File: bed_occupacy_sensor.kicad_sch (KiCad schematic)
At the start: 4 parts, among them U1 mini_esp32

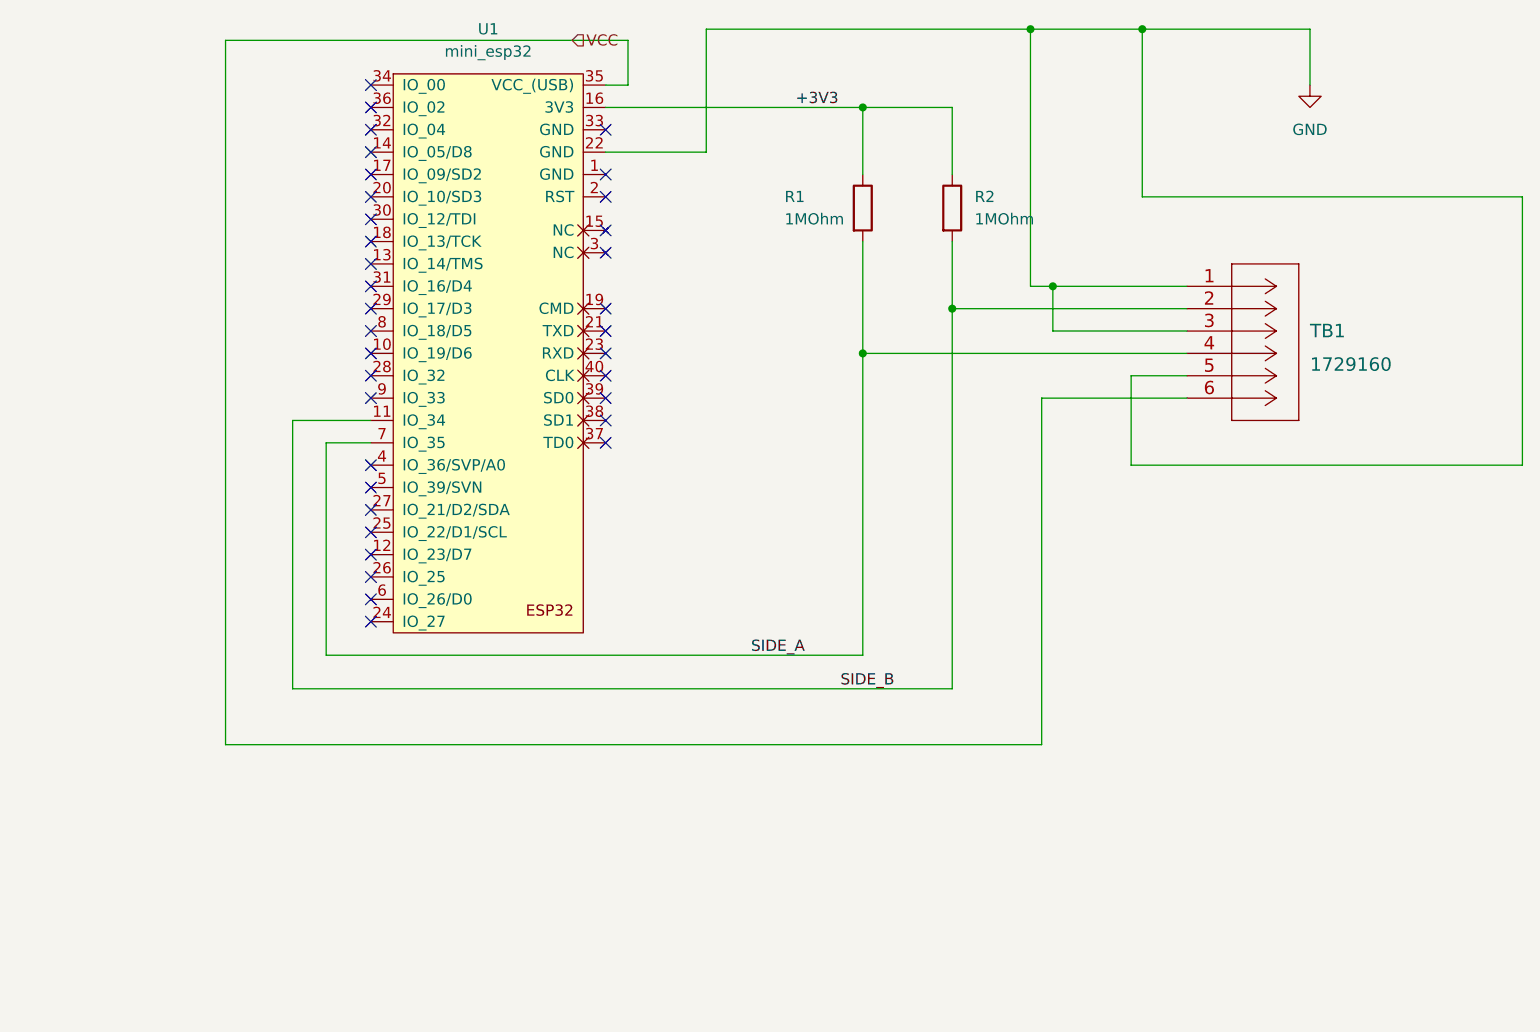
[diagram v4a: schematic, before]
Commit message: Reverse the footprint of ESP, as it was the wrong way around
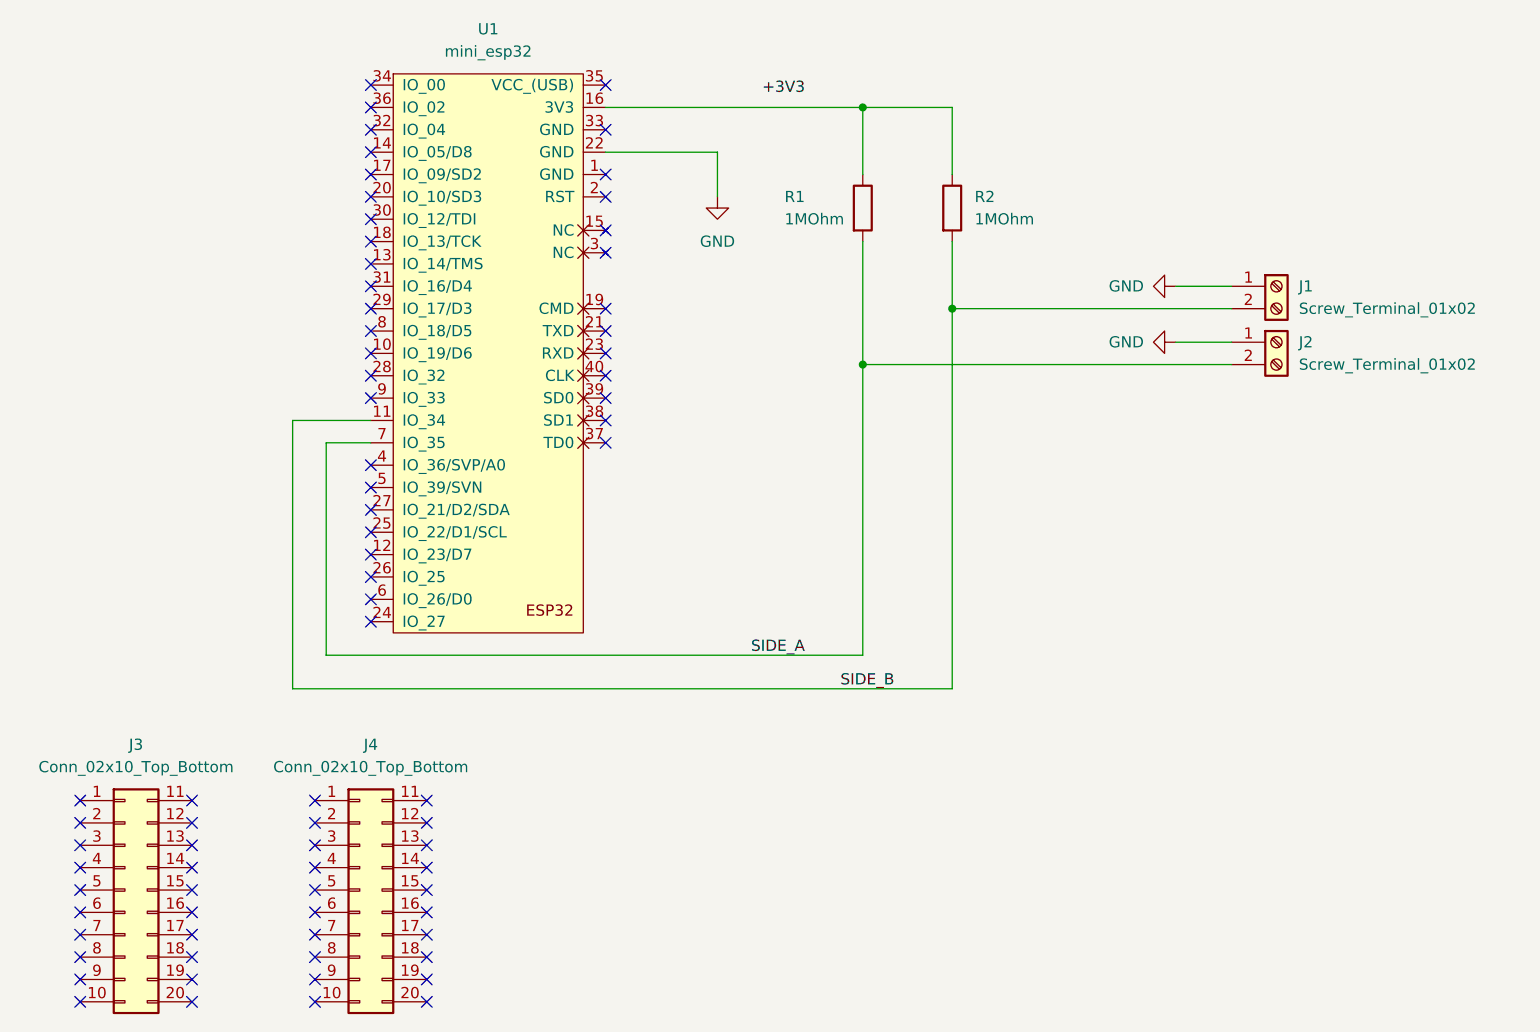
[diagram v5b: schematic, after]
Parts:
- removed TB1: 1729160, TerminalBlock_Phoenix:TerminalBlock_Phoenix_MKDS-1,5-6-5.08_1x06_P5.08mm_Horizontal, symbol phoenixcontact_1729160:1729160
- added J1, J2: Screw_Terminal_01x02, TerminalBlock_Phoenix:TerminalBlock_Phoenix_MKDS-1,5-2-5.08_1x02_P5.08mm_Horizontal, symbol Connector:Screw_Terminal_01x02
- added J3, J4: Conn_02x10_Top_Bottom, Connector_PinSocket_2.54mm:PinSocket_2x10_P2.54mm_Vertical, symbol Connector_Generic:Conn_02x10_Top_Bottom
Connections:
- net +3V3: no longer R1.1, R2.1, U1.16 (3V3)
- net GND: now also J1.1 (Pin_1), J2.1 (Pin_1)
- net SIDE_A: now also J2.2 (Pin_2)
- net SIDE_B: now also J1.2 (Pin_2)
- net VCC: no longer names the net of U1.35 (VCC_(USB))
- new net: R1.1, R2.1, U1.16 (3V3)
- no-connect marks 35 -> 76

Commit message: fixed design flaw of ESP-Pin orientation (it was the wrong way around). Now the antenna is free (on it's downside) removed QR Code because it's too small to read by a QR-Code-Reader. Updated the resistor footprint to a smaller one (10,4mm) because it fits better to standard metal-film resistors
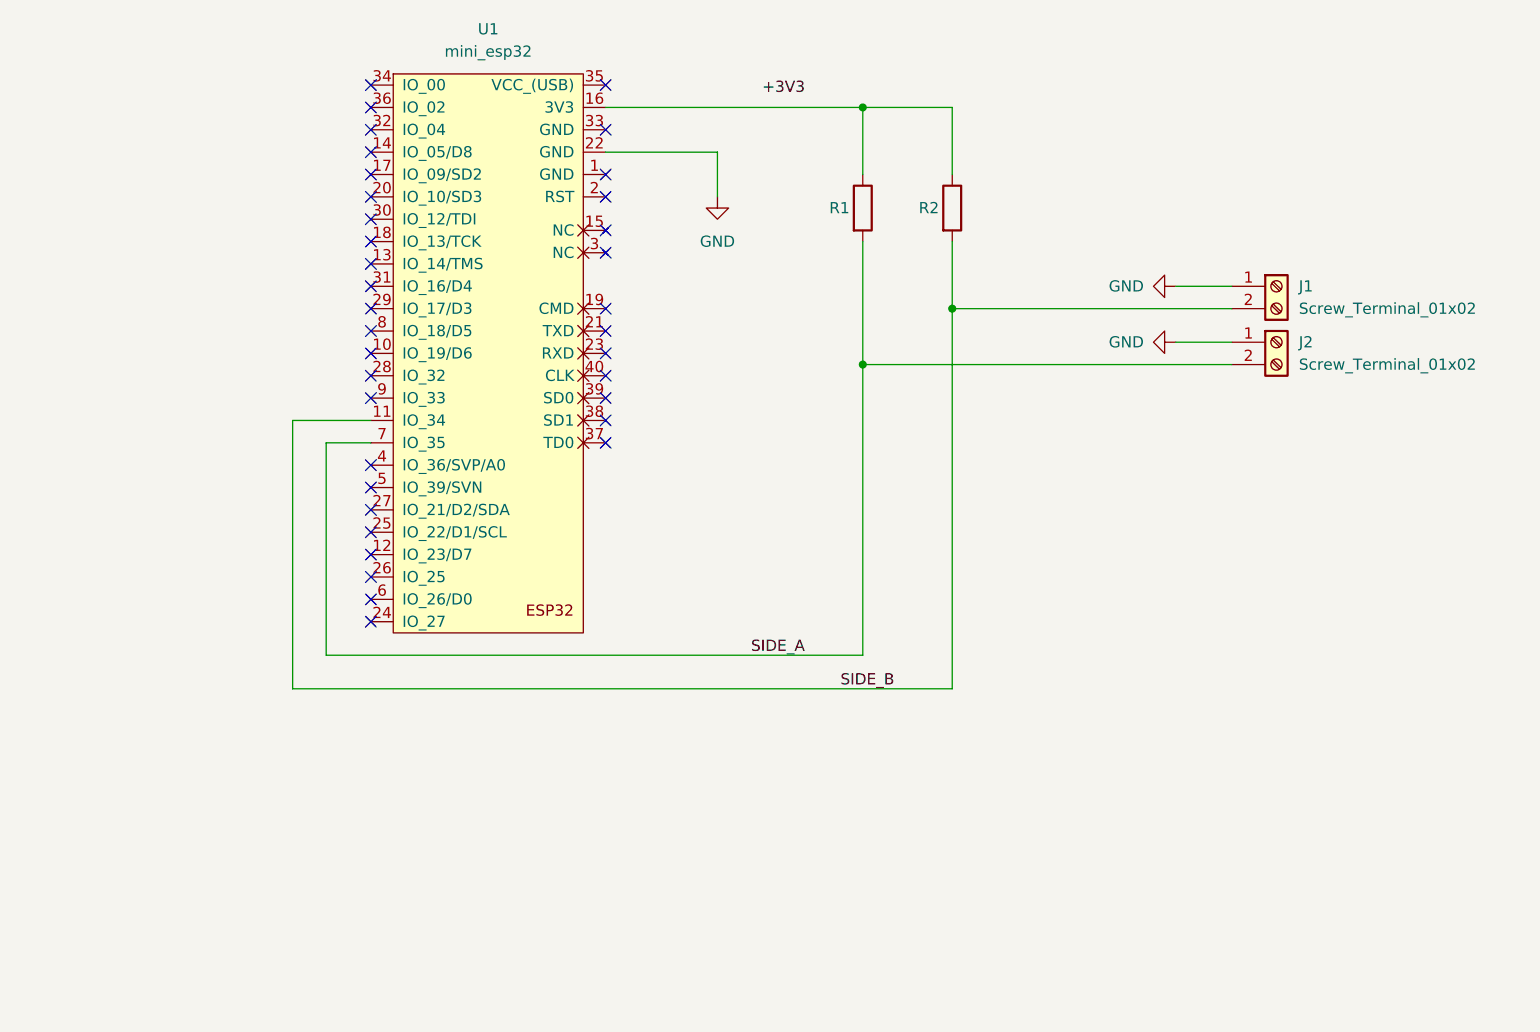
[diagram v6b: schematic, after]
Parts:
- removed J3, J4: Conn_02x10_Top_Bottom, Connector_PinSocket_2.54mm:PinSocket_2x10_P2.54mm_Vertical, symbol Connector_Generic:Conn_02x10_Top_Bottom
- R1, R2: value 1MOhm -> to be calculated; footprint Resistor_THT:R_Axial_DIN0207_L6.3mm_D2.5mm_P15.24mm_Horizontal -> Resistor_THT:R_Axial_DIN0207_L6.3mm_D2.5mm_P10.16mm_Horizontal
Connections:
- no-connect marks 76 -> 36
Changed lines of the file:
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@@
   )
   (no_connect (at 57.15 69.85))
+  (no_connect (at 83.82 24.13))
   (no_connect (at 57.15 26.67))
-  (no_connect (at 24.13 110.49))
-  (no_connect (at 83.82 24.13))
-  (no_connect (at 63.5 125.73))
-  (no_connect (at 24.13 113.03))
-  (no_connect (at 36.83 105.41))
-  (no_connect (at 63.5 113.03))
-  (no_connect (at 63.5 123.19))
-  (no_connect (at 36.83 115.57))
-  (no_connect (at 50.8 120.65))
   (no_connect (at 57.15 59.69))
-  (no_connect (at 50.8 118.11))
   (no_connect (at 57.15 57.15))
   (no_connect (at 83.82 64.77))
@@
   (no_connect (at 57.15 77.47))
   (no_connect (at 83.82 59.69))
-  (no_connect (at 63.5 107.95))
   (no_connect (at 57.15 36.83))
   (no_connect (at 57.15 29.21))
   (no_connect (at 83.82 29.21))
-  (no_connect (at 24.13 123.19))
-  (no_connect (at 36.83 107.95))
-  (no_connect (at 63.5 110.49))
   (no_connect (at 83.82 54.61))
   (no_connect (at 57.15 74.93))
-  (no_connect (at 24.13 128.27))
   (no_connect (at 83.82 52.07))
-  (no_connect (at 63.5 128.27))
-  (no_connect (at 36.83 120.65))
   (no_connect (at 83.82 62.23))
-  (no_connect (at 50.8 105.41))
   (no_connect (at 57.15 52.07))
-  (no_connect (at 36.83 118.11))
-  (no_connect (at 50.8 125.73))
-  (no_connect (at 63.5 120.65))
-  (no_connect (at 36.83 128.27))
-  (no_connect (at 24.13 107.95))
-  (no_connect (at 63.5 118.11))
-  (no_connect (at 36.83 125.73))
   (no_connect (at 83.82 40.64))
   (no_connect (at 57.15 80.01))
   (no_connect (at 57.15 54.61))
-  (no_connect (at 24.13 105.41))
   (no_connect (at 57.15 41.91))
-  (no_connect (at 24.13 125.73))
-  (no_connect (at 24.13 118.11))
-  (no_connect (at 50.8 123.19))
-  (no_connect (at 50.8 113.03))
-  (no_connect (at 36.83 123.19))
-  (no_connect (at 63.5 105.41))
   (no_connect (at 57.15 31.75))
   (no_connect (at 57.15 72.39))
   (no_connect (at 57.15 44.45))
-  (no_connect (at 24.13 120.65))
-  (no_connect (at 24.13 115.57))
-  (no_connect (at 50.8 107.95))
   (no_connect (at 57.15 34.29))
   (no_connect (at 83.82 57.15))
@@
   (no_connect (at 57.15 39.37))
   (no_connect (at 83.82 34.29))
-  (no_connect (at 36.83 110.49))
-  (no_connect (at 63.5 115.57))
-  (no_connect (at 50.8 128.27))
-  (no_connect (at 50.8 110.49))
   (no_connect (at 83.82 49.53))
   (no_connect (at 57.15 49.53))
-  (no_connect (at 50.8 115.57))
   (no_connect (at 57.15 85.09))
   (no_connect (at 83.82 43.18))
   (no_connect (at 83.82 36.83))
-  (no_connect (at 36.83 113.03))
   (no_connect (at 57.15 24.13))
   (no_connect (at 57.15 67.31))
@@
     (pin "9")
   )
-  (symbol (lib_id "Connector_Generic:Conn_02x10_Top_Bottom") (at 55.88 115.57 0) (unit 1)
-    (in_bom yes) (on_board yes) (fields_autoplaced)
-    (property "Reference" "J4" (id 0) (at 57.15 99.06 0))
-    (property "Value" "Conn_02x10_Top_Bottom" (id 1) (at 57.15 101.6 0))
-    (property "Footprint" "Connector_PinSocket_2.54mm:PinSocket_2x10_P2.54mm_Vertical" (id 2) (at 55.88 115.57 0)
-      (effects (font (size 1.27 1.27)) hide)
-    )
-    (property "Datasheet" "~" (id 3) (at 55.88 115.57 0)
-      (effects (font (size 1.27 1.27)) hide)
-    )
-    (pin "1")
-    (pin "10")
-    (pin "11")
-    (pin "12")
-    (pin "13")
-    (pin "14")
-    (pin "15")
-    (pin "16")
-    (pin "17")
-    (pin "18")
-    (pin "19")
-    (pin "2")
-    (pin "20")
-    (pin "3")
-    (pin "4")
-    (pin "5")
-    (pin "6")
-    (pin "7")
-    (pin "8")
-    (pin "9")
-  )
   (symbol (lib_id "Connector:Screw_Terminal_01x02") (at 160.02 53.34 0) (unit 1)
     (in_bom yes) (on_board yes) (fields_autoplaced)
@@
   (symbol (lib_id "Device:R") (at 113.03 38.1 0) (unit 1)
     (in_bom yes) (on_board yes)
-    (property "Reference" "R1" (id 0) (at 104.14 36.83 0)
-      (effects (font (size 1.27 1.27)) (justify left))
-    )
-    (property "Value" "1MOhm" (id 1) (at 104.14 39.37 0)
-      (effects (font (size 1.27 1.27)) (justify left))
-    )
-    (property "Footprint" "Resistor_THT:R_Axial_DIN0207_L6.3mm_D2.5mm_P15.24mm_Horizontal" (id 2) (at 111.252 38.1 90)
+    (property "Reference" "R1" (id 0) (at 109.22 38.1 0)
+      (effects (font (size 1.27 1.27)) (justify left))
+    )
+    (property "Value" "to be calculated" (id 1) (at 109.22 45.72 90)
+      (effects (font (size 1.27 1.27)) (justify left) hide)
+    )
+    (property "Footprint" "Resistor_THT:R_Axial_DIN0207_L6.3mm_D2.5mm_P10.16mm_Horizontal" (id 2) (at 111.252 38.1 90)
       (effects (font (size 1.27 1.27)) hide)
     )
@@
   )
   (symbol (lib_id "Device:R") (at 123.19 38.1 0) (unit 1)
-    (in_bom yes) (on_board yes) (fields_autoplaced)
-    (property "Reference" "R2" (id 0) (at 125.73 36.8299 0)
-      (effects (font (size 1.27 1.27)) (justify left))
-    )
-    (property "Value" "1MOhm" (id 1) (at 125.73 39.3699 0)
-      (effects (font (size 1.27 1.27)) (justify left))
-    )
-    (property "Footprint" "Resistor_THT:R_Axial_DIN0207_L6.3mm_D2.5mm_P15.24mm_Horizontal" (id 2) (at 121.412 38.1 90)
+    (in_bom yes) (on_board yes)
+    (property "Reference" "R2" (id 0) (at 119.38 38.1 0)
+      (effects (font (size 1.27 1.27)) (justify left))
+    )
+    (property "Value" "to be calculated" (id 1) (at 125.73 39.3699 0)
+      (effects (font (size 1.27 1.27)) (justify left) hide)
+    )
+    (property "Footprint" "Resistor_THT:R_Axial_DIN0207_L6.3mm_D2.5mm_P10.16mm_Horizontal" (id 2) (at 121.412 38.1 90)
       (effects (font (size 1.27 1.27)) hide)
     )
@@
     )
     (pin "1")
-  )
-  (symbol (lib_id "Connector_Generic:Conn_02x10_Top_Bottom") (at 29.21 115.57 0) (unit 1)
-    (in_bom yes) (on_board yes) (fields_autoplaced)
-    (property "Reference" "J3" (id 0) (at 30.48 99.06 0))
-    (property "Value" "Conn_02x10_Top_Bottom" (id 1) (at 30.48 101.6 0))
-    (property "Footprint" "Connector_PinSocket_2.54mm:PinSocket_2x10_P2.54mm_Vertical" (id 2) (at 29.21 115.57 0)
-      (effects (font (size 1.27 1.27)) hide)
-    )
-    (property "Datasheet" "~" (id 3) (at 29.21 115.57 0)
-      (effects (font (size 1.27 1.27)) hide)
-    )
-    (pin "1")
-    (pin "10")
-    (pin "11")
-    (pin "12")
-    (pin "13")
-    (pin "14")
-    (pin "15")
-    (pin "16")
-    (pin "17")
-    (pin "18")
-    (pin "19")
-    (pin "2")
-    (pin "20")
-    (pin "3")
-    (pin "4")
-    (pin "5")
-    (pin "6")
-    (pin "7")
-    (pin "8")
-    (pin "9")
   )
   (sheet_instances
@@
       (reference "J2") (unit 1) (value "Screw_Terminal_01x02") (footprint "TerminalBlock_Phoenix:TerminalBlock_Phoenix_MKDS-1,5-2-5.08_1x02_P5.08mm_Horizontal")
     )
-    (path "/bf0ad13e-3630-434f-91e5-05a32787e2d2"
-      (reference "J3") (unit 1) (value "Conn_02x10_Top_Bottom") (footprint "Connector_PinSocket_2.54mm:PinSocket_2x10_P2.54mm_Vertical")
-    )
-    (path "/1b9917bd-7f1c-4a3c-aa24-db0d7f60507b"
-      (reference "J4") (unit 1) (value "Conn_02x10_Top_Bottom") (footprint "Connector_PinSocket_2.54mm:PinSocket_2x10_P2.54mm_Vertical")
-    )
     (path "/34513afa-65fd-4100-9268-ca482871ddd0"
-      (reference "R1") (unit 1) (value "1MOhm") (footprint "Resistor_THT:R_Axial_DIN0207_L6.3mm_D2.5mm_P15.24mm_Horizontal")
+      (reference "R1") (unit 1) (value "to be calculated") (footprint "Resistor_THT:R_Axial_DIN0207_L6.3mm_D2.5mm_P10.16mm_Horizontal")
     )
     (path "/3d4cb2b8-b9d4-4f01-8fe6-fc15b4eb5524"
-      (reference "R2") (unit 1) (value "1MOhm") (footprint "Resistor_THT:R_Axial_DIN0207_L6.3mm_D2.5mm_P15.24mm_Horizontal")
+      (reference "R2") (unit 1) (value "to be calculated") (footprint "Resistor_THT:R_Axial_DIN0207_L6.3mm_D2.5mm_P10.16mm_Horizontal")
     )
     (path "/07c47862-40a1-4c8a-b5c1-af5fb92beb2b"
